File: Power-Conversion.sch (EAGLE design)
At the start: 45 parts, among them Q1 SUM90P10-19L, U7 LM2678

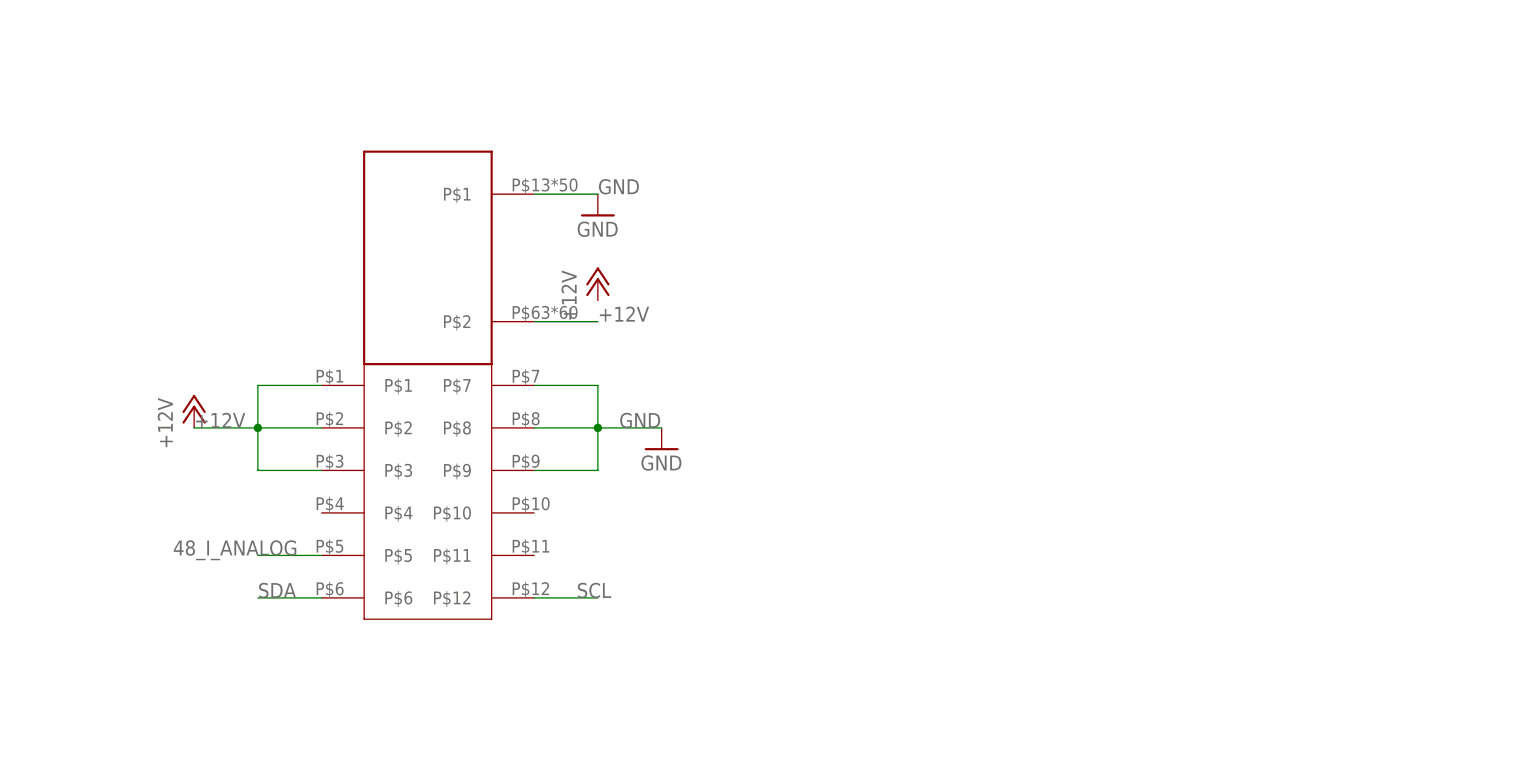
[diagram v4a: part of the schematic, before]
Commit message: Fixed to work with new connector part
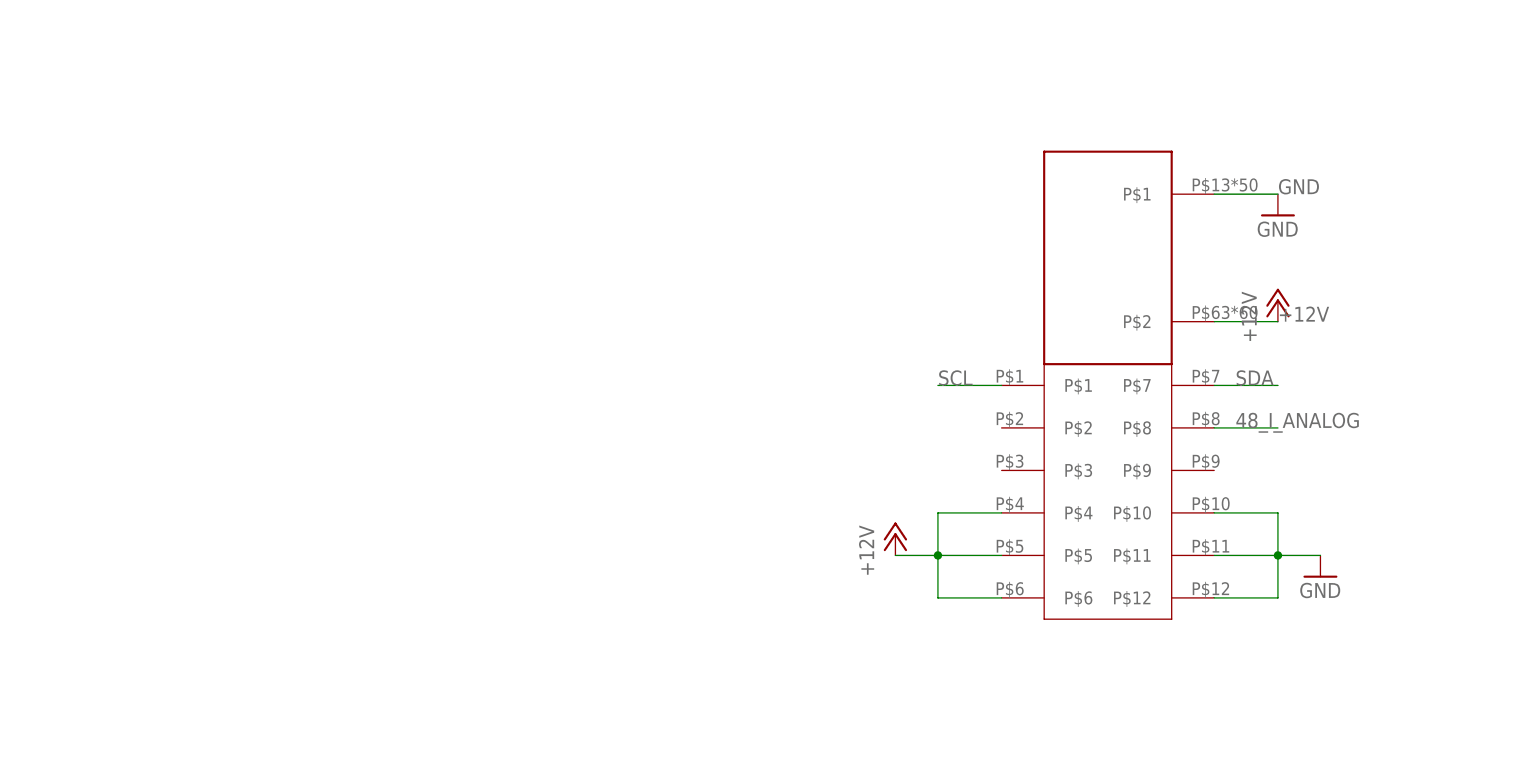
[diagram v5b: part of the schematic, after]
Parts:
- removed U$3: ESC-FULL, MotherboardParts:ESC-FULL
- added U$8: ESC-FULL, MotherboardParts:ESC-FULL
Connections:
- net +12V: now also U$8G$1.P$2, U$8G$2.P$4, U$8G$2.P$5, U$8G$2.P$6; no longer U$3G$1.P$2, U$3G$2.P$1, U$3G$2.P$2, U$3G$2.P$3
- net 48_I_ANALOG: now also U$8G$2.P$8; no longer U$3G$2.P$5
- net GND: now also U$8G$1.P$1, U$8G$2.P$10, U$8G$2.P$11, U$8G$2.P$12; no longer U$3G$1.P$1, U$3G$2.P$7, U$3G$2.P$8, U$3G$2.P$9
- net SCL: now also U$8G$2.P$1; no longer U$3G$2.P$12
- net SDA: now also U$8G$2.P$7; no longer U$3G$2.P$6
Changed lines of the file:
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@@
 <part name="J1" library="SparkFun-Connectors" deviceset="BANANA_CONN" device=""/>
 <part name="J2" library="SparkFun-Connectors" deviceset="BANANA_CONN" device=""/>
-<part name="GND6" library="supply1" deviceset="GND" device=""/>
 <part name="U$2" library="diode" deviceset="DIODE" device=""/>
 <part name="U$18" library="diode" deviceset="DIODE" device=""/>
 <part name="U$19" library="diode" deviceset="DIODE" device=""/>
-<part name="GND5" library="supply1" deviceset="GND" device=""/>
 <part name="U$20" library="MotherBoardParts2" deviceset="BRICK_TO_POWER_DIST_WHOLE" device=""/>
 <part name="U$21" library="MotherBoardParts2" deviceset="BRICK_TO_POWER_DIST_WHOLE" device=""/>
@@
 <part name="P+9" library="supply1" deviceset="+12V" device=""/>
 <part name="P+13" library="supply1" deviceset="+12V" device=""/>
-<part name="P+14" library="supply1" deviceset="+12V" device=""/>
-<part name="P+15" library="supply1" deviceset="+12V" device=""/>
 <part name="R15" library="resistor" deviceset="R-US_" device="R0603" value="0R"/>
 <part name="R5" library="resistor" deviceset="R-US_" device="R0603" value="0R"/>
@@
 <part name="F7" library="PowerComponents" deviceset="PTC(2920L)" device="" value="10A"/>
 <part name="P+18" library="supply1" deviceset="+12V" device=""/>
-<part name="U$3" library="MotherboardParts" deviceset="ESC-FULL" device=""/>
+<part name="GND21" library="supply1" deviceset="GND" device=""/>
+<part name="GND22" library="supply1" deviceset="GND" device=""/>
+<part name="P+23" library="supply1" deviceset="+12V" device=""/>
+<part name="P+24" library="supply1" deviceset="+12V" device=""/>
+<part name="U$8" library="MotherboardParts" deviceset="ESC-FULL" device=""/>
 </parts>
 <sheets>
@@
 <instance part="J1" gate="G$1" x="33.02" y="104.14"/>
 <instance part="J2" gate="G$1" x="33.02" y="99.06"/>
-<instance part="GND6" gate="1" x="248.92" y="365.76"/>
 <instance part="U$2" gate="G$1" x="53.34" y="447.04"/>
 <instance part="U$18" gate="G$1" x="142.24" y="441.96"/>
 <instance part="U$19" gate="G$1" x="233.68" y="441.96"/>
-<instance part="GND5" gate="1" x="256.54" y="337.82"/>
 <instance part="U$20" gate="G$1" x="50.8" y="482.6"/>
 <instance part="U$21" gate="G$1" x="139.7" y="482.6"/>
@@
 <instance part="P+9" gate="1" x="233.68" y="462.28"/>
 <instance part="P+13" gate="1" x="320.04" y="462.28"/>
-<instance part="P+14" gate="1" x="200.66" y="342.9"/>
-<instance part="P+15" gate="1" x="248.92" y="358.14"/>
 <instance part="R15" gate="G$1" x="187.96" y="520.7" rot="R180"/>
 <instance part="R5" gate="G$1" x="187.96" y="510.54" rot="R180"/>
@@
 <instance part="F7" gate="G$1" x="246.38" y="238.76" rot="MR90"/>
 <instance part="P+18" gate="1" x="246.38" y="251.46"/>
-<instance part="U$3" gate="G$1" x="228.6" y="360.68"/>
-<instance part="U$3" gate="G$2" x="226.06" y="327.66"/>
+<instance part="GND21" gate="1" x="330.2" y="365.76"/>
+<instance part="GND22" gate="1" x="335.28" y="322.58"/>
+<instance part="P+23" gate="1" x="284.48" y="327.66"/>
+<instance part="P+24" gate="1" x="330.2" y="355.6"/>
+<instance part="U$8" gate="G$1" x="309.88" y="360.68"/>
+<instance part="U$8" gate="G$2" x="307.34" y="327.66"/>
 </instances>
 <busses>
@@
 </segment>
 <segment>
-<pinref part="U$3" gate="G$1" pin="P$1"/>
-<wire x1="241.3" y1="368.3" x2="248.92" y2="368.3" width="0.1524" layer="91"/>
-<label x="248.92" y="368.3" size="1.778" layer="95"/>
-<pinref part="GND6" gate="1" pin="GND"/>
-</segment>
-<segment>
-<pinref part="U$3" gate="G$2" pin="P$7"/>
-<wire x1="241.3" y1="345.44" x2="248.92" y2="345.44" width="0.1524" layer="91"/>
-<pinref part="U$3" gate="G$2" pin="P$9"/>
-<wire x1="241.3" y1="335.28" x2="248.92" y2="335.28" width="0.1524" layer="91"/>
-<wire x1="248.92" y1="345.44" x2="248.92" y2="340.36" width="0.1524" layer="91"/>
-<pinref part="U$3" gate="G$2" pin="P$8"/>
-<wire x1="248.92" y1="340.36" x2="248.92" y2="335.28" width="0.1524" layer="91"/>
-<wire x1="241.3" y1="340.36" x2="248.92" y2="340.36" width="0.1524" layer="91"/>
-<junction x="248.92" y="340.36"/>
-<wire x1="248.92" y1="340.36" x2="256.54" y2="340.36" width="0.1524" layer="91"/>
-<label x="251.46" y="340.36" size="1.778" layer="95"/>
-<pinref part="GND5" gate="1" pin="GND"/>
+<pinref part="U$8" gate="G$1" pin="P$1"/>
+<wire x1="322.58" y1="368.3" x2="330.2" y2="368.3" width="0.1524" layer="91"/>
+<label x="330.2" y="368.3" size="1.778" layer="95"/>
+<pinref part="GND21" gate="1" pin="GND"/>
+</segment>
+<segment>
+<pinref part="U$8" gate="G$2" pin="P$12"/>
+<wire x1="322.58" y1="320.04" x2="330.2" y2="320.04" width="0.1524" layer="91"/>
+<pinref part="U$8" gate="G$2" pin="P$11"/>
+<wire x1="322.58" y1="325.12" x2="330.2" y2="325.12" width="0.1524" layer="91"/>
+<wire x1="330.2" y1="325.12" x2="330.2" y2="320.04" width="0.1524" layer="91"/>
+<pinref part="U$8" gate="G$2" pin="P$10"/>
+<wire x1="322.58" y1="330.2" x2="330.2" y2="330.2" width="0.1524" layer="91"/>
+<wire x1="330.2" y1="330.2" x2="330.2" y2="325.12" width="0.1524" layer="91"/>
+<junction x="330.2" y="325.12"/>
+<wire x1="330.2" y1="325.12" x2="335.28" y2="325.12" width="0.1524" layer="91"/>
+<pinref part="GND22" gate="1" pin="GND"/>
 </segment>
 </net>
@@
 </segment>
 <segment>
-<pinref part="U$3" gate="G$1" pin="P$2"/>
-<wire x1="241.3" y1="353.06" x2="248.92" y2="353.06" width="0.1524" layer="91"/>
-<label x="248.92" y="353.06" size="1.778" layer="95"/>
-</segment>
-<segment>
-<pinref part="U$3" gate="G$2" pin="P$1"/>
-<wire x1="215.9" y1="345.44" x2="208.28" y2="345.44" width="0.1524" layer="91"/>
-<pinref part="U$3" gate="G$2" pin="P$3"/>
-<wire x1="215.9" y1="335.28" x2="208.28" y2="335.28" width="0.1524" layer="91"/>
-<wire x1="208.28" y1="345.44" x2="208.28" y2="340.36" width="0.1524" layer="91"/>
-<pinref part="U$3" gate="G$2" pin="P$2"/>
-<wire x1="208.28" y1="340.36" x2="208.28" y2="335.28" width="0.1524" layer="91"/>
-<wire x1="215.9" y1="340.36" x2="208.28" y2="340.36" width="0.1524" layer="91"/>
-<junction x="208.28" y="340.36"/>
-<wire x1="208.28" y1="340.36" x2="200.66" y2="340.36" width="0.1524" layer="91"/>
-<label x="200.66" y="340.36" size="1.778" layer="95"/>
-<pinref part="P+14" gate="1" pin="+12V"/>
+<pinref part="U$8" gate="G$1" pin="P$2"/>
+<wire x1="322.58" y1="353.06" x2="330.2" y2="353.06" width="0.1524" layer="91"/>
+<label x="330.2" y="353.06" size="1.778" layer="95"/>
+<pinref part="P+24" gate="1" pin="+12V"/>
+</segment>
+<segment>
+<pinref part="U$8" gate="G$2" pin="P$4"/>
+<wire x1="297.18" y1="330.2" x2="289.56" y2="330.2" width="0.1524" layer="91"/>
+<wire x1="289.56" y1="330.2" x2="289.56" y2="325.12" width="0.1524" layer="91"/>
+<pinref part="U$8" gate="G$2" pin="P$6"/>
+<wire x1="289.56" y1="325.12" x2="289.56" y2="320.04" width="0.1524" layer="91"/>
+<wire x1="289.56" y1="320.04" x2="297.18" y2="320.04" width="0.1524" layer="91"/>
+<pinref part="U$8" gate="G$2" pin="P$5"/>
+<wire x1="297.18" y1="325.12" x2="289.56" y2="325.12" width="0.1524" layer="91"/>
+<junction x="289.56" y="325.12"/>
+<wire x1="289.56" y1="325.12" x2="284.48" y2="325.12" width="0.1524" layer="91"/>
+<pinref part="P+23" gate="1" pin="+12V"/>
 </segment>
 </net>
@@
 </segment>
 <segment>
-<pinref part="U$3" gate="G$2" pin="P$12"/>
-<wire x1="241.3" y1="320.04" x2="248.92" y2="320.04" width="0.1524" layer="91"/>
-<label x="246.38" y="320.04" size="1.778" layer="95"/>
+<pinref part="U$8" gate="G$2" pin="P$1"/>
+<wire x1="297.18" y1="345.44" x2="289.56" y2="345.44" width="0.1524" layer="91"/>
+<label x="289.56" y="345.44" size="1.778" layer="95"/>
 </segment>
 </net>
@@
 </segment>
 <segment>
-<pinref part="U$3" gate="G$2" pin="P$6"/>
-<wire x1="215.9" y1="320.04" x2="208.28" y2="320.04" width="0.1524" layer="91"/>
-<label x="208.28" y="320.04" size="1.778" layer="95"/>
+<pinref part="U$8" gate="G$2" pin="P$7"/>
+<wire x1="322.58" y1="345.44" x2="330.2" y2="345.44" width="0.1524" layer="91"/>
+<label x="325.12" y="345.44" size="1.778" layer="95"/>
 </segment>
 </net>
@@
 </segment>
 <segment>
-<pinref part="U$3" gate="G$2" pin="P$5"/>
-<wire x1="215.9" y1="325.12" x2="208.28" y2="325.12" width="0.1524" layer="91"/>
-<label x="198.12" y="325.12" size="1.778" layer="95"/>
-</segment>
-</net>
+<pinref part="U$8" gate="G$2" pin="P$8"/>
+<wire x1="322.58" y1="340.36" x2="330.2" y2="340.36" width="0.1524" layer="91"/>
+<label x="325.12" y="340.36" size="1.778" layer="95"/>
+</segment>
+</net>

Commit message: Cleaning up
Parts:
- added JP1, JP2: (no value), pinhead:PINHD-1X1
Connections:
- net SCL: now also JP1.1
- net SDA: now also JP2.1
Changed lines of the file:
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@@
 <part name="P+24" library="supply1" deviceset="+12V" device=""/>
 <part name="U$8" library="MotherboardParts" deviceset="ESC-FULL" device=""/>
+<part name="JP1" library="pinhead" library_urn="urn:adsk.eagle:library:325" deviceset="PINHD-1X1" device="" package3d_urn="urn:adsk.eagle:package:22485/2"/>
+<part name="JP2" library="pinhead" library_urn="urn:adsk.eagle:library:325" deviceset="PINHD-1X1" device="" package3d_urn="urn:adsk.eagle:package:22485/2"/>
 </parts>
 <sheets>
@@
 <instance part="U$8" gate="G$1" x="309.88" y="360.68"/>
 <instance part="U$8" gate="G$2" x="307.34" y="327.66"/>
+<instance part="JP1" gate="G$1" x="88.9" y="337.82"/>
+<instance part="JP2" gate="G$1" x="88.9" y="317.5"/>
 </instances>
 <busses>
@@
 <label x="289.56" y="345.44" size="1.778" layer="95"/>
 </segment>
+<segment>
+<pinref part="JP1" gate="G$1" pin="1"/>
+<wire x1="86.36" y1="337.82" x2="96.52" y2="337.82" width="0.1524" layer="91"/>
+</segment>
 </net>
 <net name="SDA" class="0">
@@
 <wire x1="322.58" y1="345.44" x2="330.2" y2="345.44" width="0.1524" layer="91"/>
 <label x="325.12" y="345.44" size="1.778" layer="95"/>
+</segment>
+<segment>
+<pinref part="JP2" gate="G$1" pin="1"/>
+<wire x1="86.36" y1="317.5" x2="96.52" y2="317.5" width="0.1524" layer="91"/>
 </segment>
 </net>
@@
 will not be understood (or retained) with this version.
 </note>
+<note version="8.3" severity="warning">
+Since Version 8.3, EAGLE supports the association of 3D packages
+with devices in libraries, schematics, and board files. Those 3D
+packages will not be understood (or retained) with this version.
+</note>
 </compatibility>

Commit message: Version submitted to elecrow
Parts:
- added J3: (no value), SparkFun-Connectors:BANANA_CONN
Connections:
- net VCC: now also J3.1
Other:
- note added: "/Users/kingj/Desktop/kirby.bmp"

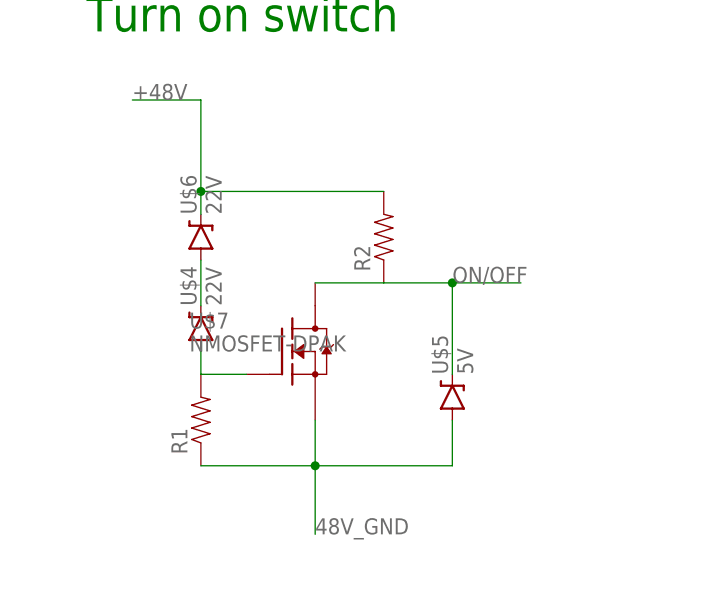
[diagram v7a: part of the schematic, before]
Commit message: Put in resistor values on ON/OFF switch
on ON/OFF switch
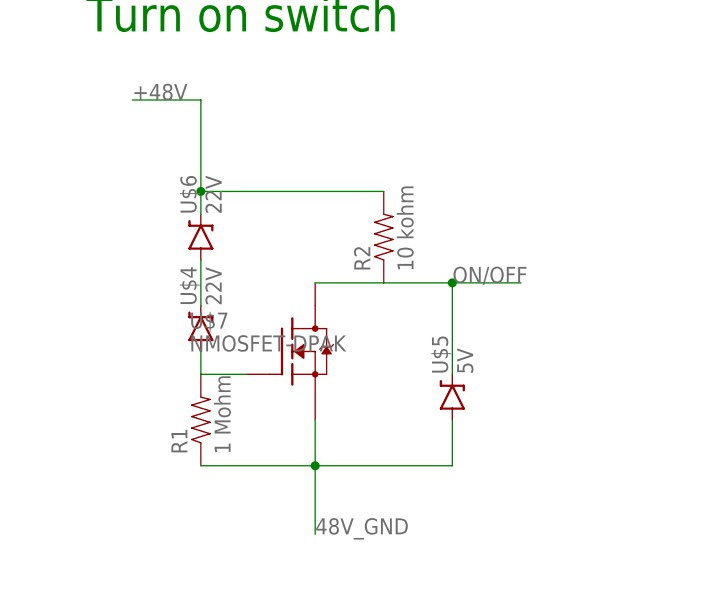
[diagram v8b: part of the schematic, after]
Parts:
- R1: value (none) -> 1 Mohm
- R2: value (none) -> 10 kohm
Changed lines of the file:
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@@
 <setting verticaltext="up"/>
 </settings>
-<grid distance="1" unitdist="mil" unit="mil" style="lines" multiple="1" display="yes" altdistance="0.01" altunitdist="inch" altunit="inch"/>
+<grid distance="0.1" unitdist="inch" unit="inch" style="lines" multiple="1" display="no" altdistance="0.01" altunitdist="inch" altunit="inch"/>
 <layers>
 <layer number="1" name="Top" color="4" fill="1" visible="no" active="no"/>
@@
 <attribute name="PN-DIGI" value="BZX84C22LT1GOSCT-ND"/>
 </part>
-<part name="R1" library="SparkFun-Passives" deviceset="RESISTOR" device="0603-RES"/>
-<part name="R2" library="SparkFun-Passives" deviceset="RESISTOR" device="0603-RES"/>
+<part name="R1" library="SparkFun-Passives" deviceset="RESISTOR" device="0603-RES" value="1 Mohm"/>
+<part name="R2" library="SparkFun-Passives" deviceset="RESISTOR" device="0603-RES" value="10 kohm"/>
 <part name="U$7" library="MotherboardParts" deviceset="NMOSFET-DPAK" device=""/>
 <part name="U$9" library="PowerComponents" deviceset="SWITCHMODE_SCHOTTKY" device=""/>
